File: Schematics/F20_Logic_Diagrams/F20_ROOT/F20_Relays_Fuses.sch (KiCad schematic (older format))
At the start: 23 parts, among them K2 MicroRelay, K3 MicroRelay, K4 MicroRelay, K5 MicroRelay, K6 MicroRelay, K7 MicroRelay

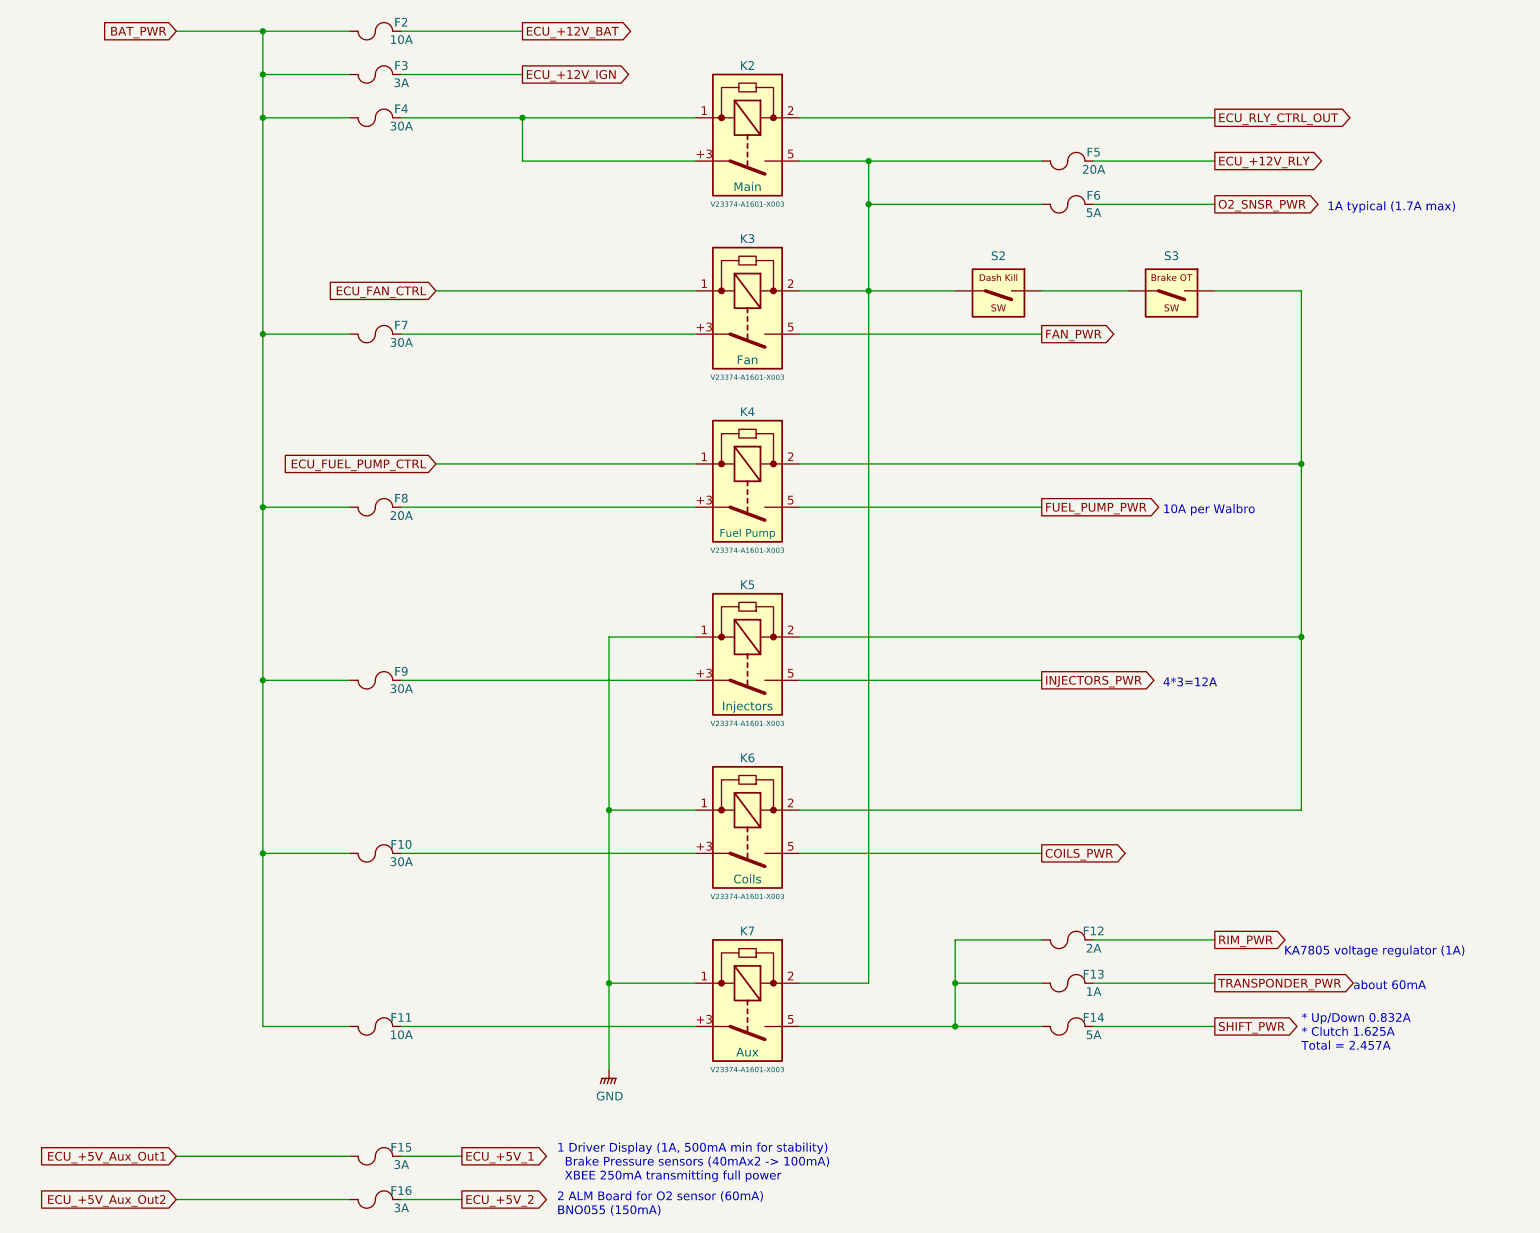
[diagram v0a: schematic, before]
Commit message: Re-annotated Logic Diagrams, pulled a BOM list based on Logic Diagrams
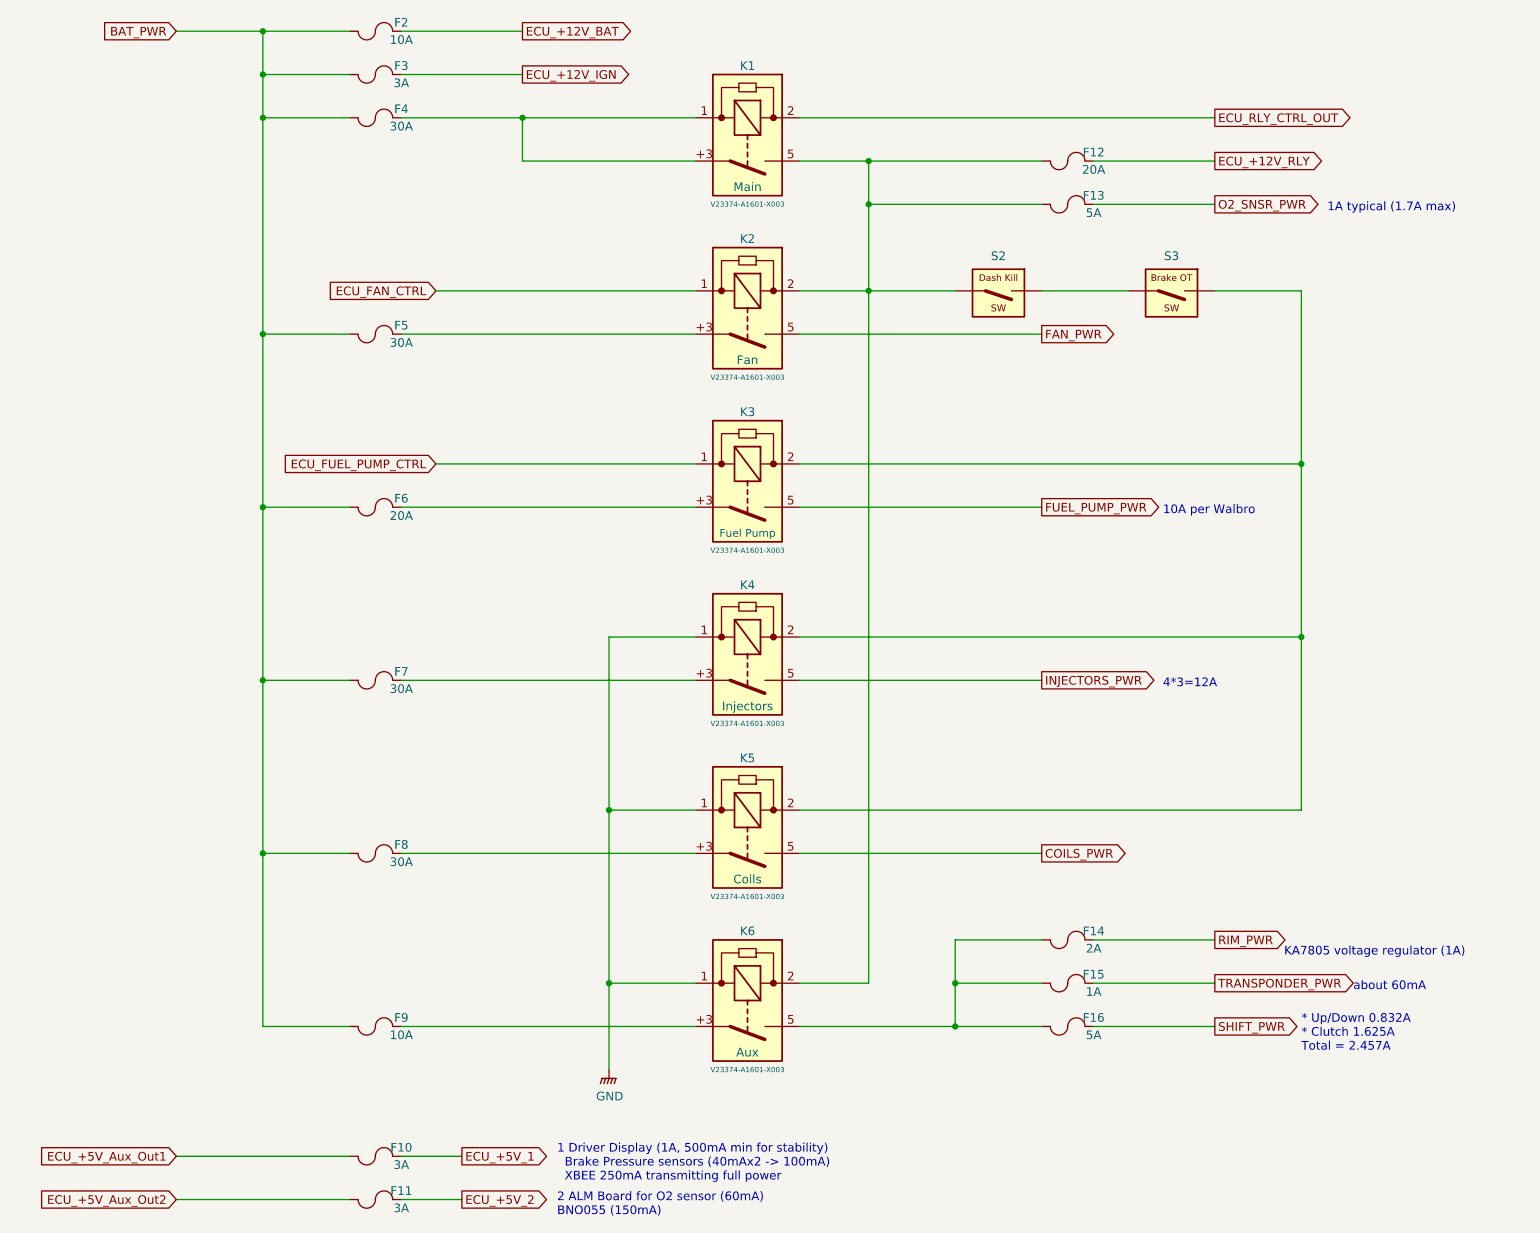
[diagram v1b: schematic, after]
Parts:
- renumbered F15 to F10, F16 to F11, F5 to F12, F6 to F13, F12 to F14, F13 to F15, F14 to F16, F7 to F5, F8 to F6, F9 to F7, F10 to F8, F11 to F9, K2 to K1, K3 to K2, K4 to K3, K5 to K4, K6 to K5, K7 to K6
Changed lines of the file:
@@
 $Descr A 11000 8500
 encoding utf-8
-Sheet 11 18
+Sheet 3 18
 Title "Relays and Fuses"
 Date "2020-03-04"
@@
 $EndDescr
 $Comp
-L FSAE_Library:MicroRelay K2
+L FSAE_Library:MicroRelay K1
 U 1 1 5E342D8D
 P 5000 1500
-F 0 "K2" H 5300 1800 50  0000 C CNN
+F 0 "K1" H 5300 1800 50  0000 C CNN
 F 1 "MicroRelay" H 5100 1800 50  0001 L CNN
 F 2 "" H 5100 950 50  0001 L CNN
@@
 $EndComp
 $Comp
-L FSAE_Library:MicroRelay K3
+L FSAE_Library:MicroRelay K2
 U 1 1 5E3476EA
 P 5000 2500
-F 0 "K3" H 5300 2800 50  0000 C CNN
+F 0 "K2" H 5300 2800 50  0000 C CNN
 F 1 "MicroRelay" H 5100 2800 50  0001 L CNN
 F 2 "" H 5100 1950 50  0001 L CNN
@@
 $EndComp
 $Comp
-L FSAE_Library:MicroRelay K4
+L FSAE_Library:MicroRelay K3
 U 1 1 5E3482B5
 P 5000 3500
-F 0 "K4" H 5300 3800 50  0000 C CNN
+F 0 "K3" H 5300 3800 50  0000 C CNN
 F 1 "MicroRelay" H 5100 3800 50  0001 L CNN
 F 2 "" H 5100 2950 50  0001 L CNN
@@
 $EndComp
 $Comp
-L FSAE_Library:MicroRelay K5
+L FSAE_Library:MicroRelay K4
 U 1 1 5E3492F0
 P 5000 4500
-F 0 "K5" H 5300 4800 50  0000 C CNN
+F 0 "K4" H 5300 4800 50  0000 C CNN
 F 1 "MicroRelay" H 5100 4800 50  0001 L CNN
 F 2 "" H 5100 3950 50  0001 L CNN
@@
 $EndComp
 $Comp
-L FSAE_Library:MicroRelay K7
+L FSAE_Library:MicroRelay K6
 U 1 1 5E3498B4
 P 5000 6500
-F 0 "K7" H 5300 6800 50  0000 C CNN
+F 0 "K6" H 5300 6800 50  0000 C CNN
 F 1 "MicroRelay" H 5100 6800 50  0001 L CNN
 F 2 "" H 5100 5950 50  0001 L CNN
@@
 	5000 4500 4500 4500
 $Comp
-L FSAE_Library:Fuse F7
+L FSAE_Library:Fuse F5
 U 1 1 5E3B4200
 P 3000 2750
-F 0 "F7" H 3300 2800 50  0000 C CNN
+F 0 "F5" H 3300 2800 50  0000 C CNN
 F 1 "30A" H 3300 2700 50  0000 C CNN
 F 2 "" H 3150 2830 50  0001 C CNN
@@
 	3000 2750 2500 2750
 $Comp
-L FSAE_Library:Fuse F8
+L FSAE_Library:Fuse F6
 U 1 1 5E3BE26F
 P 3000 3750
-F 0 "F8" H 3300 3800 50  0000 C CNN
+F 0 "F6" H 3300 3800 50  0000 C CNN
 F 1 "20A" H 3300 3700 50  0000 C CNN
 F 2 "" H 3150 3830 50  0001 C CNN
@@
 Connection ~ 2500 2750
 $Comp
-L FSAE_Library:Fuse F9
+L FSAE_Library:Fuse F7
 U 1 1 5E3BFFD4
 P 3000 4750
-F 0 "F9" H 3300 4800 50  0000 C CNN
+F 0 "F7" H 3300 4800 50  0000 C CNN
 F 1 "30A" H 3300 4700 50  0000 C CNN
 F 2 "" H 3150 4830 50  0001 C CNN
@@
 Connection ~ 2500 3750
 $Comp
-L FSAE_Library:Fuse F11
+L FSAE_Library:Fuse F9
 U 1 1 5E3C1EE5
 P 3000 6750
-F 0 "F11" H 3300 6800 50  0000 C CNN
+F 0 "F9" H 3300 6800 50  0000 C CNN
 F 1 "10A" H 3300 6700 50  0000 C CNN
 F 2 "" H 3150 6830 50  0001 C CNN
@@
 	3300 6750 5000 6750
 $Comp
-L FSAE_Library:Fuse F13
+L FSAE_Library:Fuse F15
 U 1 1 5E3E18E2
 P 7000 6500
-F 0 "F13" H 7300 6550 50  0000 C CNN
+F 0 "F15" H 7300 6550 50  0000 C CNN
 F 1 "1A" H 7300 6450 50  0000 C CNN
 F 2 "" H 7150 6580 50  0001 C CNN
@@
 ECU_+12V_RLY
 $Comp
-L FSAE_Library:Fuse F5
+L FSAE_Library:Fuse F12
 U 1 1 5E442A66
 P 7000 1750
-F 0 "F5" H 7300 1800 50  0000 C CNN
+F 0 "F12" H 7300 1800 50  0000 C CNN
 F 1 "20A" H 7300 1700 50  0000 C CNN
 F 2 "" H 7150 1830 50  0001 C CNN
@@
 O2_SNSR_PWR
 $Comp
-L FSAE_Library:Fuse F14
+L FSAE_Library:Fuse F16
 U 1 1 5E3C06C7
 P 7000 6750
-F 0 "F14" H 7300 6800 50  0000 C CNN
+F 0 "F16" H 7300 6800 50  0000 C CNN
 F 1 "5A" H 7300 6700 50  0000 C CNN
 F 2 "" H 7150 6830 50  0001 C CNN
@@
 $EndComp
 $Comp
-L FSAE_Library:GND #PWR02
+L FSAE_Library:GND #PWR06
 U 1 1 5E3C4736
 P 4500 7000
-F 0 "#PWR02" H 4500 6800 50  0001 C CNN
+F 0 "#PWR06" H 4500 6800 50  0001 C CNN
 F 1 "GND" H 4504 6846 50  0000 C CNN
 F 2 "" H 4500 6950 50  0001 C CNN
@@
 ECU_+5V_Aux_Out1
 $Comp
-L FSAE_Library:Fuse F15
+L FSAE_Library:Fuse F10
 U 1 1 5E3EDD00
 P 3000 7500
-F 0 "F15" H 3300 7550 50  0000 C CNN
+F 0 "F10" H 3300 7550 50  0000 C CNN
 F 1 "3A" H 3300 7450 50  0000 C CNN
 F 2 "" H 3150 7580 50  0001 C CNN
@@
 	6000 1750 6000 2000
 $Comp
-L FSAE_Library:Fuse F6
+L FSAE_Library:Fuse F13
 U 1 1 5E471A10
 P 7000 2000
-F 0 "F6" H 7300 2050 50  0000 C CNN
+F 0 "F13" H 7300 2050 50  0000 C CNN
 F 1 "5A" H 7300 1950 50  0000 C CNN
 F 2 "" H 7150 2080 50  0001 C CNN
@@
 KA7805 voltage regulator (1A)
 $Comp
-L FSAE_Library:Fuse F12
+L FSAE_Library:Fuse F14
 U 1 1 5E3E15AD
 P 7000 6250
-F 0 "F12" H 7300 6300 50  0000 C CNN
+F 0 "F14" H 7300 6300 50  0000 C CNN
 F 1 "2A" H 7300 6200 50  0000 C CNN
 F 2 "" H 7150 6330 50  0001 C CNN
@@
 ECU_+5V_Aux_Out2
 $Comp
-L FSAE_Library:Fuse F16
+L FSAE_Library:Fuse F11
 U 1 1 5E60DDBF
 P 3000 7750
-F 0 "F16" H 3300 7800 50  0000 C CNN
+F 0 "F11" H 3300 7800 50  0000 C CNN
 F 1 "3A" H 3300 7700 50  0000 C CNN
 F 2 "" H 3150 7830 50  0001 C CNN
@@
 4*3=12A
 $Comp
-L FSAE_Library:MicroRelay K6
+L FSAE_Library:MicroRelay K5
 U 1 1 5E6B03C6
 P 5000 5500
-F 0 "K6" H 5300 5800 50  0000 C CNN
+F 0 "K5" H 5300 5800 50  0000 C CNN
 F 1 "MicroRelay" H 5100 5800 50  0001 L CNN
 F 2 "" H 5100 4950 50  0001 L CNN
@@
 	4500 5500 4500 6500
 $Comp
-L FSAE_Library:Fuse F10
+L FSAE_Library:Fuse F8
 U 1 1 5E6CE263
 P 3000 5750
-F 0 "F10" H 3300 5800 50  0000 C CNN
+F 0 "F8" H 3300 5800 50  0000 C CNN
 F 1 "30A" H 3300 5700 50  0000 C CNN
 F 2 "" H 3150 5830 50  0001 C CNN
